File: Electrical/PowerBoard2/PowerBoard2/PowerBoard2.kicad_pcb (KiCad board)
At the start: 2 copper layers, 14 parts, among them J1 XT60PW-M, J2 XT60PW-M, J3 B4B-XH-A_LF__SN_, J5 XT60PW-M, U1 LMZ22005TZ/NOPB, U2 INA226AIDGSR, U3 USB-A-S-RA-TSMT

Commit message: pullup resistors
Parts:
- added R3: 10k, Resistor_SMD:R_0805_2012Metric_Pad1.20x1.40mm_HandSolder, F.Cu at (192.5, 76.5)
- added R4: 10k, Resistor_SMD:R_0805_2012Metric_Pad1.20x1.40mm_HandSolder, F.Cu at (190.0, 76.5)
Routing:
- net Net-(U2-VS): track 26.2 -> 34.9 mm, vias 1 -> 2
- net /SCL: track 19.8 -> 23.3 mm, vias 1 -> 2
- net /SDA: track 20.7 -> 21.8 mm, vias 1 -> 2

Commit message: remove via
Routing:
- net Net-(U2-VS): vias 2 -> 1
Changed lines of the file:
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@@
-	)
-	(via
-		(at 191.5 67.35)
-		(size 0.3)
-		(drill 0.2)
-		(layers "F.Cu" "B.Cu")
-		(net 8)
 	)
 	(via

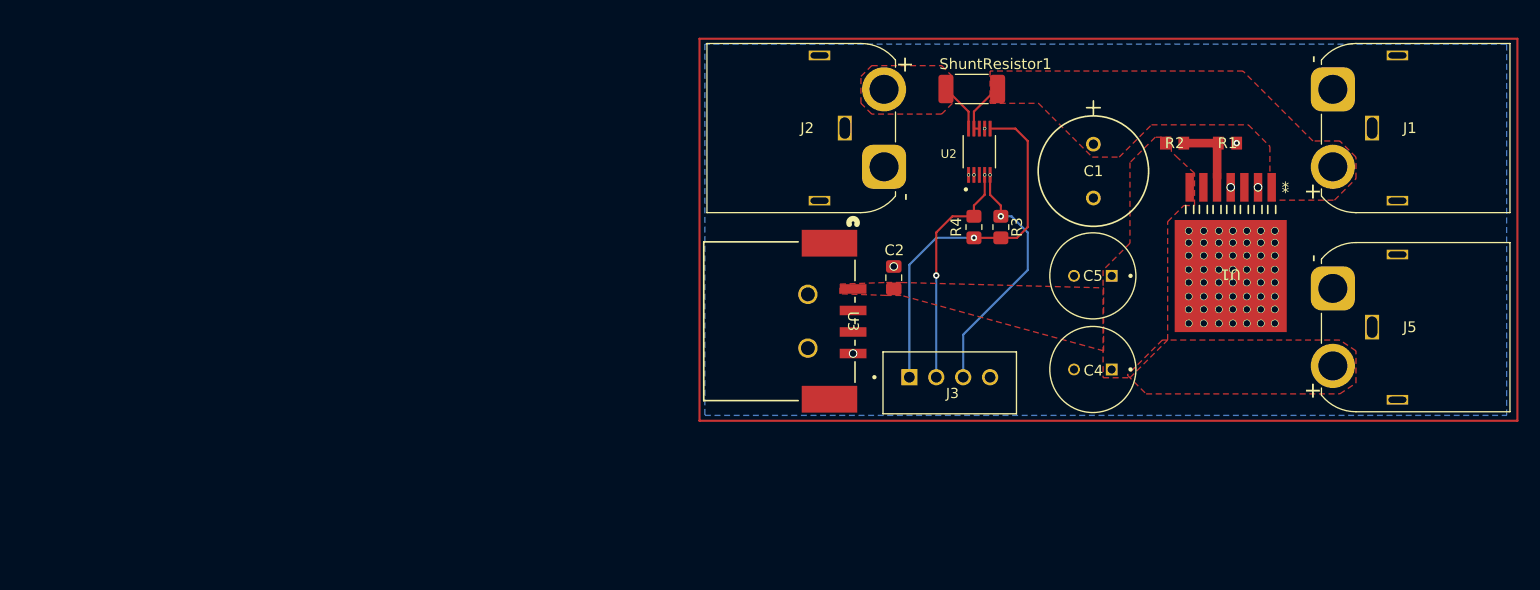
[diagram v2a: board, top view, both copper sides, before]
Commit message: widened traces for 5V output
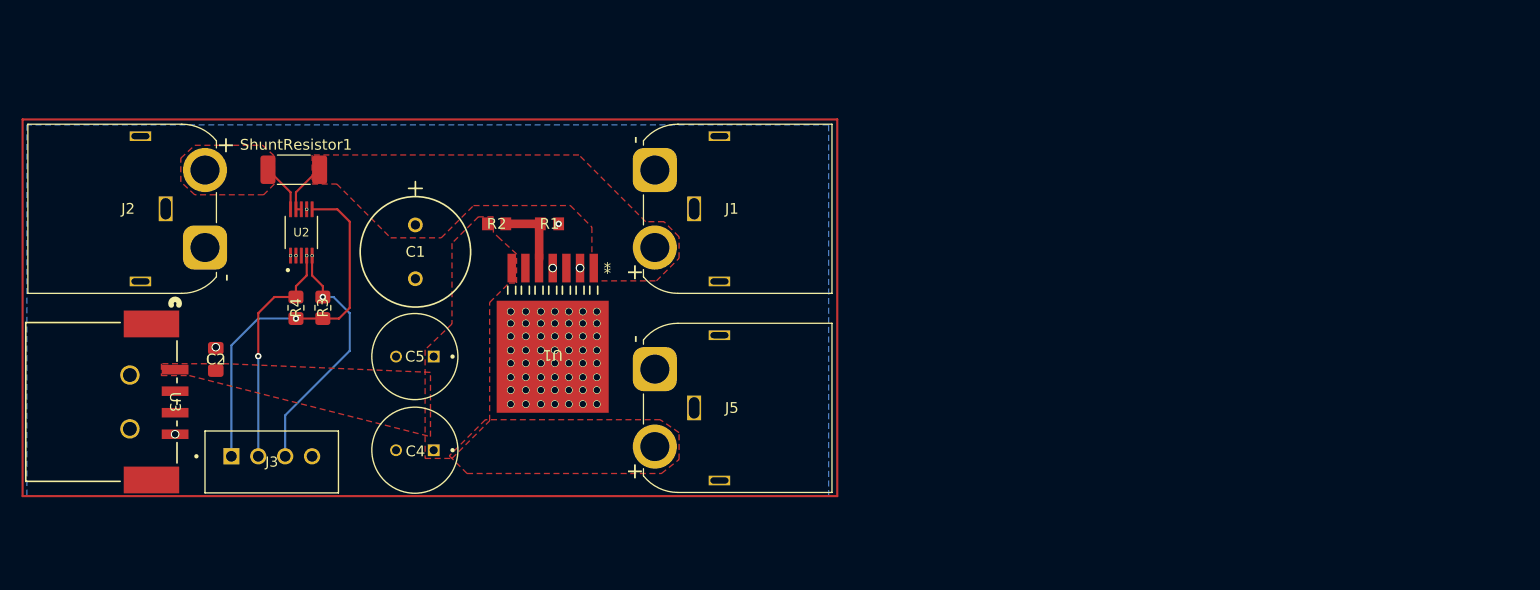
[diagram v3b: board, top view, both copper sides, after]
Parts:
- moved J2 63.5 mm to (118.5, 78.4)
- moved C2 63.5 mm to (119.5, 88.8)
- moved C1 63.4 mm to (138.1, 76.3)
- moved C4 63.4 mm to (138.1, 97.2)
- moved C5 63.4 mm to (138.1, 88.5)
- moved J1 63.4 mm to (160.3, 71.2)
- moved J5 63.4 mm to (160.3, 89.7)
- moved R1 63.4 mm to (150.6, 76.2)
- moved R2 63.4 mm to (145.6, 76.2)
- moved R3 63.4 mm to (129.5, 84.0)
- moved R4 63.4 mm to (127.0, 84.0)
- moved ShuntResistor1 63.4 mm to (126.8, 71.2)
- moved U1 63.4 mm to (150.9, 88.4)
- moved U2 63.4 mm to (127.5, 77.0)
- moved U3 63.4 mm to (115.8, 89.8)
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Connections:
- net Net-(U2-VS) renamed +3.3V

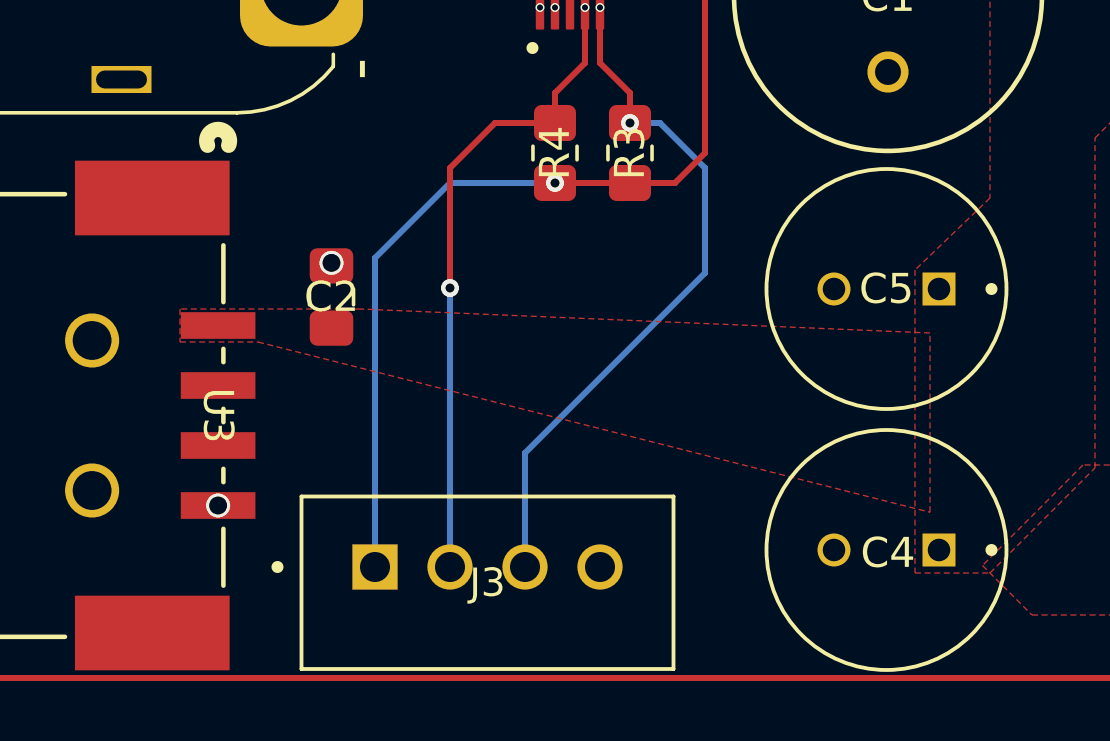
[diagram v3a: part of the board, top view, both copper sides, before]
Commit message: stabilizing capacitors
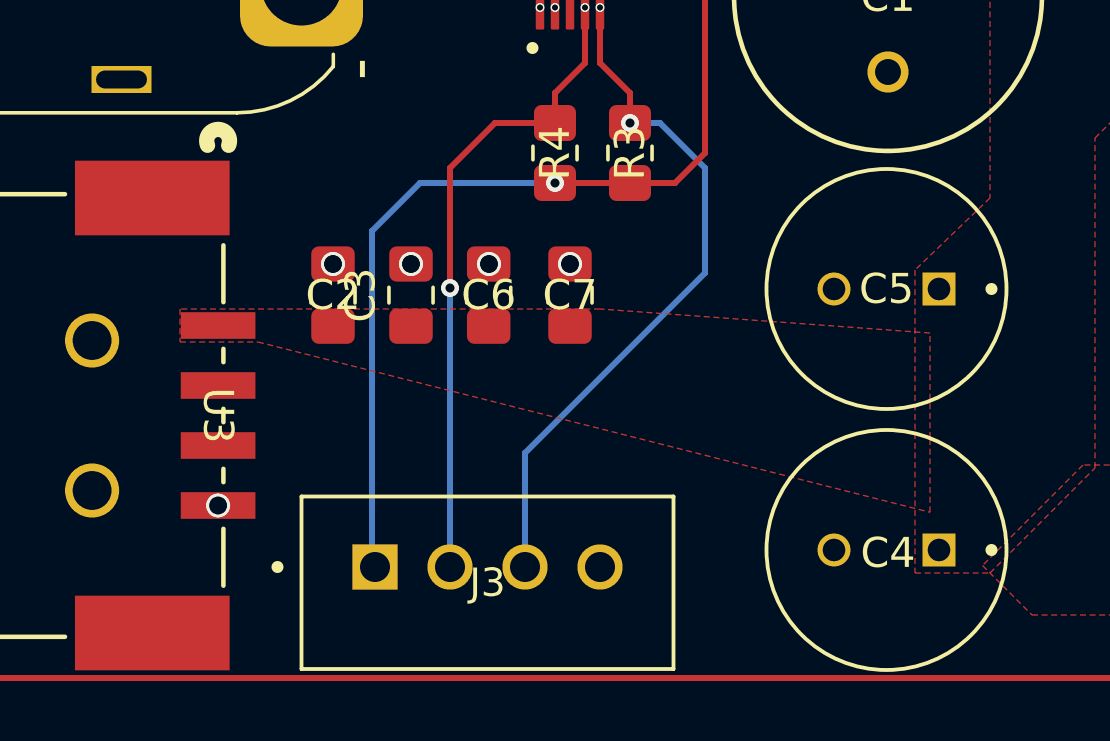
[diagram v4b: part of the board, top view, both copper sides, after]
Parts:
- added C3: 100uF, Capacitor_SMD:C_0805_2012Metric_Pad1.18x1.45mm_HandSolder, F.Cu at (122.2, 88.7)
- added C6: 10uF, Capacitor_SMD:C_0805_2012Metric_Pad1.18x1.45mm_HandSolder, F.Cu at (124.8, 88.7)
- added C7: 0.1uF, Capacitor_SMD:C_0805_2012Metric_Pad1.18x1.45mm_HandSolder, F.Cu at (127.5, 88.7)
- C2: value 300uF -> 100uF
- moved C2 0.08 mm to (119.6, 88.7)
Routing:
- net +3.3V: track 34.9 -> 35.5 mm
- net GND: vias 64 -> 67

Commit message: bypass capacitor
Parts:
- added C8: 0.1uF, Capacitor_SMD:C_0805_2012Metric_Pad1.18x1.45mm_HandSolder, F.Cu at (130.6, 75.9)
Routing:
- net GND: vias 67 -> 68
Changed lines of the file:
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@@
 		)
 	)
+	(footprint "Capacitor_SMD:C_0805_2012Metric_Pad1.18x1.45mm_HandSolder"
+		(layer "F.Cu")
+		(at 130.6 75.9 -90)
+		(descr "Capacitor SMD 0805 (2012 Metric), square (rectangular) end terminal, IPC_7351 nominal with elongated pad for handsoldering. (Body size source: IPC-SM-782 page 76, https://www.pcb-3d.com/wordpress/wp-content/uploads/ipc-sm-782a_amendment_1_and_2.pdf, https://docs.google.com/spreadsheets/d/1BsfQQcO9C6DZCsRaXUlFlo91Tg2WpOkGARC1WS5S8t0/edit?usp=sharing), generated with kicad-footprint-generator")
+		(tags "capacitor handsolder")
+		(property "Reference" "C8"
+			(at 0 0 90)
+			(layer "F.SilkS")
+			(effects
+				(font
+					(size 1 1)
+					(thickness 0.15)
+				)
+			)
+		)
+		(property "Value" "0.1uF"
+			(at 0 1.68 90)
+			(layer "F.Fab")
+			(effects
+				(font
+					(size 1 1)
+					(thickness 0.15)
+				)
+			)
+		)
+		(property "Footprint" "Capacitor_SMD:C_0805_2012Metric_Pad1.18x1.45mm_HandSolder"
+			(at 0 0 -90)
+			(unlocked yes)
+			(layer "F.Fab")
+			(hide yes)
+			(effects
+				(font
+					(size 1.27 1.27)
+					(thickness 0.15)
+				)
+			)
+		)
+		(property "Datasheet" ""
+			(at 0 0 -90)
+			(unlocked yes)
+			(layer "F.Fab")
+			(hide yes)
+			(effects
+				(font
+					(size 1.27 1.27)
+					(thickness 0.15)
+				)
+			)
+		)
+		(property "Description" "Unpolarized capacitor"
+			(at 0 0 -90)
+			(unlocked yes)
+			(layer "F.Fab")
+			(hide yes)
+			(effects
+				(font
+					(size 1.27 1.27)
+					(thickness 0.15)
+				)
+			)
+		)
+		(property ki_fp_filters "C_*")
+		(sheetname "Root")
+		(sheetfile "PowerBoard2.kicad_sch")
+		(attr smd)
+		(fp_line
+			(start -0.261252 0.735)
+			(end 0.261252 0.735)
+			(stroke
+				(width 0.12)
+				(type solid)
+			)
+			(layer "F.SilkS")
+		)
+		(fp_line
+			(start -0.261252 -0.735)
+			(end 0.261252 -0.735)
+			(stroke
+				(width 0.12)
+				(type solid)
+			)
+			(layer "F.SilkS")
+		)
+		(fp_line
+			(start -1.88 0.98)
+			(end -1.88 -0.98)
+			(stroke
+				(width 0.05)
+				(type solid)
+			)
+			(layer "F.CrtYd")
+		)
+		(fp_line
+			(start 1.88 0.98)
+			(end -1.88 0.98)
+			(stroke
+				(width 0.05)
+				(type solid)
+			)
+			(layer "F.CrtYd")
+		)
+		(fp_line
+			(start -1.88 -0.98)
+			(end 1.88 -0.98)
+			(stroke
+				(width 0.05)
+				(type solid)
+			)
+			(layer "F.CrtYd")
+		)
+		(fp_line
+			(start 1.88 -0.98)
+			(end 1.88 0.98)
+			(stroke
+				(width 0.05)
+				(type solid)
+			)
+			(layer "F.CrtYd")
+		)
+		(fp_line
+			(start -1 0.625)
+			(end -1 -0.625)
+			(stroke
+				(width 0.1)
+				(type solid)
+			)
+			(layer "F.Fab")
+		)
+		(fp_line
+			(start 1 0.625)
+			(end -1 0.625)
+			(stroke
+				(width 0.1)
+				(type solid)
+			)
+			(layer "F.Fab")
+		)
+		(fp_line
+			(start -1 -0.625)
+			(end 1 -0.625)
+			(stroke
+				(width 0.1)
+				(type solid)
+			)
+			(layer "F.Fab")
+		)
+		(fp_line
+			(start 1 -0.625)
+			(end 1 0.625)
+			(stroke
+				(width 0.1)
+				(type solid)
+			)
+			(layer "F.Fab")
+		)
+		(fp_text user "${REFERENCE}"
+			(at 0 0 90)
+			(layer "F.Fab")
+			(effects
+				(font
+					(size 0.5 0.5)
+					(thickness 0.08)
+				)
+			)
+		)
+		(pad "1" smd roundrect
+			(at -1.0375 0 270)
+			(size 1.175 1.45)
+			(layers "F.Cu" "F.Paste" "F.Mask")
+			(roundrect_rratio 0.212766)
+			(net 8 "+3.3V")
+			(pintype "passive")
+		)
+		(pad "2" smd roundrect
+			(at 1.0375 0 270)
+			(size 1.175 1.45)
+			(layers "F.Cu" "F.Paste" "F.Mask")
+			(roundrect_rratio 0.212766)
+			(net 1 "GND")
+			(pintype "passive")
+		)
+		(model "${KICAD8_3DMODEL_DIR}/Capacitor_SMD.3dshapes/C_0805_2012Metric.wrl"
+			(offset
+				(xyz 0 0 0)
+			)
+			(scale
+				(xyz 1 1 1)
+			)
+			(rotate
+				(xyz 0 0 0)
+			)
+		)
+	)
 	(footprint "_Footprints:RC0805N_PAN"
 		(layer "F.Cu")
@@
 			)
 		)
-		(fp_text user "*"
-			(at -5.08 8.0899 180)
+		(fp_text user "${REFERENCE}"
+			(at 0 0 180)
 			(unlocked yes)
 			(layer "F.Fab")
@@
 			)
 		)
-		(fp_text user "${REFERENCE}"
-			(at 0 0 180)
+		(fp_text user "*"
+			(at -5.08 8.0899 180)
 			(unlocked yes)
 			(layer "F.Fab")
@@
 	)
 	(via
+		(at 130.6 76.9375)
+		(size 0.6)
+		(drill 0.3)
+		(layers "F.Cu" "B.Cu")
+		(net 1)
+	)
+	(via
 		(at 146.96 84.35)
 		(size 0.7)
@@
 	)
 	(segment
-		(start 129.5 85)
-		(end 131 85)
+		(start 132 76.2)
+		(end 130.65 74.85)
 		(width 0.2)
 		(layer "F.Cu")
@@
 	(segment
 		(start 132 84)
-		(end 132 76)
+		(end 132 76.2)
 		(width 0.2)
 		(layer "F.Cu")
@@
 	)
 	(segment
-		(start 132 76)
-		(end 130.85 74.85)
+		(start 130.65 74.85)
+		(end 128.5 74.85)
 		(width 0.2)
 		(layer "F.Cu")
@@
 	)
 	(segment
-		(start 130.85 74.85)
-		(end 128.5 74.85)
+		(start 129.5 85)
+		(end 131 85)
 		(width 0.2)
 		(layer "F.Cu")

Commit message: shunt
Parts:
- removed ShuntResistor1: 0.005 R, Resistor_SMD:R_2010_5025Metric_Pad1.40x2.65mm_HandSolder
- added R5: CSNL2010FT2L00, Shuntresistor:STA_CSNL2010&lessthan_=3_STP, F.Cu at (126.7, 71.2)
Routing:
- net /SDA: vias 2 -> 1
- net /SCL: vias 2 -> 1

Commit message: capacitors and opamps
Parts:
- removed C3: 100uF, Capacitor_SMD:C_0805_2012Metric_Pad1.18x1.45mm_HandSolder
- added J4: B4B-XH-A_LF__SN_, B4B-XH-A_LF__SN_:JST_B4B-XH-A_LF__SN_, F.Cu at (146.1, 60.8)
- added R6: 36k, Resistor_SMD:R_0805_2012Metric_Pad1.20x1.40mm_HandSolder, F.Cu at (147.1, 67.5)
- added R7: 33k, Resistor_SMD:R_0805_2012Metric_Pad1.20x1.40mm_HandSolder, F.Cu at (147.1, 65.3)
- added R8: 120k, Resistor_SMD:R_0805_2012Metric_Pad1.20x1.40mm_HandSolder, F.Cu at (136.6, 67.5)
- added R9: 33k, Resistor_SMD:R_0805_2012Metric_Pad1.20x1.40mm_HandSolder, F.Cu at (136.6, 65.3)
- added REF**: MountingHole_2.5mm, MountingHole:MountingHole_2.5mm, F.Cu at (104.5, 105.2)
- added REF**: MountingHole_2.5mm, MountingHole:MountingHole_2.5mm, F.Cu at (104.5, 60.4)
- added REF**: MountingHole_2.5mm, MountingHole:MountingHole_2.5mm, F.Cu at (174.5, 105.2)
- added REF**: MountingHole_2.5mm, MountingHole:MountingHole_2.5mm, F.Cu at (174.5, 60.4)
- added U4: TLV2370IDBVR, _Footprints:DBV6, F.Cu at (152.5, 66.6)
- added U5: TLV2370IDBVR, _Footprints:DBV6, F.Cu at (141.9, 66.6)
- C2: value 100uF -> 16ZLJ470MTA8X11.5; footprint Capacitor_SMD:C_0805_2012Metric_Pad1.18x1.45mm_HandSolder -> bigcapacitor:CAP_YX_8X11P5_RUB
- moved J3 6.38 mm to (124.5, 104.7)
- moved C6 3.41 mm to (128.2, 88.8)
- moved C7 3.30 mm to (130.8, 88.7)
- moved C2 3.16 mm to (122.1, 86.8), turned to -90 degrees
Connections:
- C2 pad 1: +5V -> GND
- C2 pad 2: GND -> +5V
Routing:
- net +5V: track 0.00 -> 28.1 mm, vias 0 -> 2
- net Net-(U4-IN-): track 0.00 -> 9.91 mm
- net Net-(U5-IN-): track 0.00 -> 9.89 mm
- net /SCL: track 23.3 -> 31.7 mm
- net +3.3V: track 35.4 -> 42.0 mm
- net /SDA: track 21.8 -> 28.1 mm
- net Net-(U4-IN+): track 0.00 -> 5.46 mm
- net Net-(U5-IN+): track 0.00 -> 5.36 mm
- net /Buck Converter/Vin (12V): track 4.95 -> 7.75 mm
- net GND: vias 68 -> 70

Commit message: final alignment
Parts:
- 12V, 5V reading: renamed from J4
- Current reading: renamed from J3
- renumbered J1 to 12Vin, J2 to 12Vout, J5 to 5Vout, U3 to 5Vout
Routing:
- net /SCL: track 31.7 -> 28.1 mm
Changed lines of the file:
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@@
 		(layer "F.Cu")
 		(at 124.55 104.7 180)
-		(property "Reference" "J3"
-			(at 0 0 0)
+		(property "Reference" "Current reading"
+			(at -12.2 -2.3 0)
 			(layer "F.SilkS")
 			(effects
@@
 		(tags "resistor handsolder")
 		(property "Reference" "R7"
-			(at 0 0 360)
+			(at 0 0 0)
 			(layer "F.SilkS")
 			(effects
@@
 		)
 		(property "Value" "33k"
-			(at 0 1.65 360)
+			(at 0 1.65 0)
 			(layer "F.Fab")
 			(effects
@@
 		)
 		(fp_text user "${REFERENCE}"
-			(at 0 0 360)
+			(at 0 0 0)
 			(layer "F.Fab")
 			(effects
@@
 		(tags "resistor handsolder")
 		(property "Reference" "R3"
-			(at 0 0 90)
+			(at 0 0 180)
 			(layer "F.SilkS")
 			(effects
@@
 		(descr "Connector XT60 Horizontal PCB Male, https://www.bto.pl/pdf/08988/XT60IPW-M3.pdf")
 		(tags "RC Connector XT60")
-		(property "Reference" "J1"
-			(at 3.6 -7.15 180)
+		(property "Reference" "12Vin"
+			(at -5.45 0.6 180)
 			(layer "F.SilkS")
 			(effects
@@
 		(tags "16ZLJ470MTA8X11.5 ")
 		(property "Reference" "C2"
-			(at 1.75 0 -90)
+			(at 1.75 0 0)
 			(unlocked yes)
 			(layer "F.SilkS")
@@
 		(tags "mounting hole 2.5mm no annular")
 		(property "Reference" "REF**"
-			(at 0 -3.5 0)
+			(at 4.9 0 0)
 			(layer "F.SilkS")
 			(effects
@@
 		(tags "resistor handsolder")
 		(property "Reference" "R6"
-			(at 0 0 360)
+			(at 0 0 0)
 			(layer "F.SilkS")
 			(effects
@@
 		)
 		(property "Value" "36k"
-			(at 0 1.65 360)
+			(at 0 1.65 0)
 			(layer "F.Fab")
 			(effects
@@
 		)
 		(fp_text user "${REFERENCE}"
-			(at 0 0 360)
+			(at 0 0 0)
 			(layer "F.Fab")
 			(effects
@@
 		(tags "capacitor handsolder")
 		(property "Reference" "C8"
-			(at 0 0 90)
+			(at 0 0 180)
 			(layer "F.SilkS")
 			(effects
@@
 		(tags "mounting hole 2.5mm no annular")
 		(property "Reference" "REF**"
-			(at 0 -3.5 0)
+			(at -5 0 0)
 			(layer "F.SilkS")
 			(effects
@@
 		(descr "Connector XT60 Horizontal PCB Male, https://www.bto.pl/pdf/08988/XT60IPW-M3.pdf")
 		(tags "RC Connector XT60")
-		(property "Reference" "J5"
-			(at 3.6 -7.15 180)
+		(property "Reference" "5Vout"
+			(at 12.8 0.6 180)
 			(layer "F.SilkS")
 			(effects
@@
 		(at 115.770101 89.750003 -90)
 		(tags "USB-A-S-RA-TSMT ")
-		(property "Reference" "U3"
-			(at 2.999999 0 -90)
+		(property "Reference" "5Vout"
+			(at 12.749997 0.520101 0)
 			(unlocked yes)
 			(layer "F.SilkS")
@@
 		(tags "resistor handsolder")
 		(property "Reference" "R4"
-			(at 0 0 90)
+			(at 0 0 180)
 			(layer "F.SilkS")
 			(effects
@@
 		(layer "F.Cu")
 		(at 146.05 60.775)
-		(property "Reference" "J4"
-			(at 0 0 0)
+		(property "Reference" "12V, 5V reading"
+			(at -12.55 2.225 0)
 			(layer "F.SilkS")
 			(effects
@@
 		(descr "Connector XT60 Horizontal PCB Male, https://www.bto.pl/pdf/08988/XT60IPW-M3.pdf")
 		(tags "RC Connector XT60")
-		(property "Reference" "J2"
-			(at 3.6 -7.15 180)
+		(property "Reference" "12Vout"
+			(at 12.65 -0.05 180)
 			(layer "F.SilkS")
 			(effects
@@
 		(tags "resistor handsolder")
 		(property "Reference" "R9"
-			(at 0 0 360)
+			(at 0 0 0)
 			(layer "F.SilkS")
 			(effects
@@
 		)
 		(property "Value" "33k"
-			(at 0 1.65 360)
+			(at 0 1.65 0)
 			(layer "F.Fab")
 			(effects
@@
 		)
 		(fp_text user "${REFERENCE}"
-			(at 0 0 360)
+			(at 0 0 0)
 			(layer "F.Fab")
 			(effects
@@
 	(segment
 		(start 129.5 82)
-		(end 129.5 83)
+		(end 128.5 81)
 		(width 0.2)
 		(layer "F.Cu")
@@
 	)
 	(segment
-		(start 128.5 81)
+		(start 129.5 83)
 		(end 129.5 82)
 		(width 0.2)
@@
 	)
 	(segment
-		(start 128.5 79.15)
-		(end 128.5 81)
+		(start 128.5 81)
+		(end 128.5 79.15)
 		(width 0.2)
 		(layer "F.Cu")
@@
 	)
 	(segment
-		(start 132.7 85.2)
-		(end 130.5 83)
+		(start 130.7 84.2)
+		(end 130.7 85.9)
 		(width 0.2)
 		(layer "B.Cu")
@@
 	)
 	(segment
-		(start 131.8 91.2)
-		(end 132.7 90.3)
+		(start 130.7 85.9)
+		(end 130.3 86.3)
 		(width 0.2)
 		(layer "B.Cu")
@@
 	)
 	(segment
-		(start 130.5 83)
-		(end 129.5 83)
+		(start 129.5 86.8)
+		(end 129.5 91)
 		(width 0.2)
 		(layer "B.Cu")
@@
 	)
 	(segment
-		(start 125.8 104.175)
-		(end 125.8 94.7)
+		(start 129.5 83)
+		(end 130.7 84.2)
 		(width 0.2)
 		(layer "B.Cu")
@@
 	)
 	(segment
-		(start 125.8 94.7)
-		(end 129.3 91.2)
+		(start 130 86.3)
+		(end 129.5 86.8)
 		(width 0.2)
 		(layer "B.Cu")
@@
 	)
 	(segment
-		(start 129.3 91.2)
-		(end 131.8 91.2)
+		(start 130.3 86.3)
+		(end 130 86.3)
 		(width 0.2)
 		(layer "B.Cu")
@@
 	)
 	(segment
-		(start 132.7 90.3)
-		(end 132.7 85.2)
+		(start 129.5 91)
+		(end 125.8 94.7)
 		(width 0.2)
 		(layer "B.Cu")
@@
 	)
 	(segment
-		(start 127 82)
-		(end 128 81)
+		(start 125.8 94.7)
+		(end 125.8 104.175)
 		(width 0.2)
-		(layer "F.Cu")
-		(net 10)
+		(layer "B.Cu")
+		(net 9)
 	)
 	(segment
-		(start 128 81)
-		(end 128 79.15)
+		(start 127 83)
+		(end 127 82)
 		(width 0.2)
 		(layer "F.Cu")
@@
 	)
 	(segment
-		(start 127 83)
-		(end 127 82.9)
+		(start 127 82)
+		(end 128 81)
 		(width 0.2)
 		(layer "F.Cu")
@@
 	)
 	(segment
-		(start 127 82.9)
-		(end 127 82)
+		(start 128 81)
+		(end 128 79.15)
 		(width 0.2)
 		(layer "F.Cu")
@@
 	)
 	(via
-		(at 127 82.9)
+		(at 127 83)
 		(size 0.6)
 		(drill 0.3)
@@
 	)
 	(segment
-		(start 126.9 91.1)
-		(end 126.9 86.8)
+		(start 128.2 84.2)
+		(end 128.2 85.9)
 		(width 0.2)
 		(layer "B.Cu")
@@
 	)
 	(segment
-		(start 128.2 84.1)
-		(end 127 82.9)
+		(start 127.8 86.3)
+		(end 127.4 86.3)
 		(width 0.2)
 		(layer "B.Cu")
@@
 	(segment
 		(start 126.9 86.8)
-		(end 128.2 85.5)
+		(end 126.9 91.1)
 		(width 0.2)
 		(layer "B.Cu")
@@
 	)
 	(segment
-		(start 123.3 104.175)
-		(end 123.3 94.7)
+		(start 127 83)
+		(end 128.2 84.2)
 		(width 0.2)
 		(layer "B.Cu")
@@
 	)
 	(segment
-		(start 128.2 85.5)
-		(end 128.2 84.1)
+		(start 123.3 94.7)
+		(end 123.3 104.175)
 		(width 0.2)
 		(layer "B.Cu")
@@
 	)
 	(segment
-		(start 123.3 94.7)
-		(end 126.9 91.1)
+		(start 127.4 86.3)
+		(end 126.9 86.8)
+		(width 0.2)
+		(layer "B.Cu")
+		(net 10)
+	)
+	(segment
+		(start 128.2 85.9)
+		(end 127.8 86.3)
+		(width 0.2)
+		(layer "B.Cu")
+		(net 10)
+	)
+	(segment
+		(start 126.9 91.1)
+		(end 123.3 94.7)
 		(width 0.2)
 		(layer "B.Cu")
